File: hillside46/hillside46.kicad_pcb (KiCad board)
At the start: 2 copper layers, 142.5 x 99.9 mm, 86 parts, among them J1 Haptic, J2 TRRS, J3 Bat_Pos, J4 Bat_Neg, J5 Bat_Pos, J6 Bat_Neg, K1 SW_Key, K10 SW_Key, K11 SW_Key, K12 SW_Key, K13 SW_Key, K14 SW_Key, K15 SW_Key, K16 SW_Key, K17 SW_Key, K18 SW_Key, K19 SW_Rotary, K2 SW_Key, K20 SW_Rotary, K21 SW_Key, K22 SW_Key, K23 SW_Key, K3 SW_Key, K4 SW_Key, K5 SW_Key, K6 SW_Key, K7 SW_Key, K8 SW_Key, K9 SW_Key, SW1 SKQGAFE010, SW2 SW_Power, U1 ProMicro_r, U2 SRV05-4

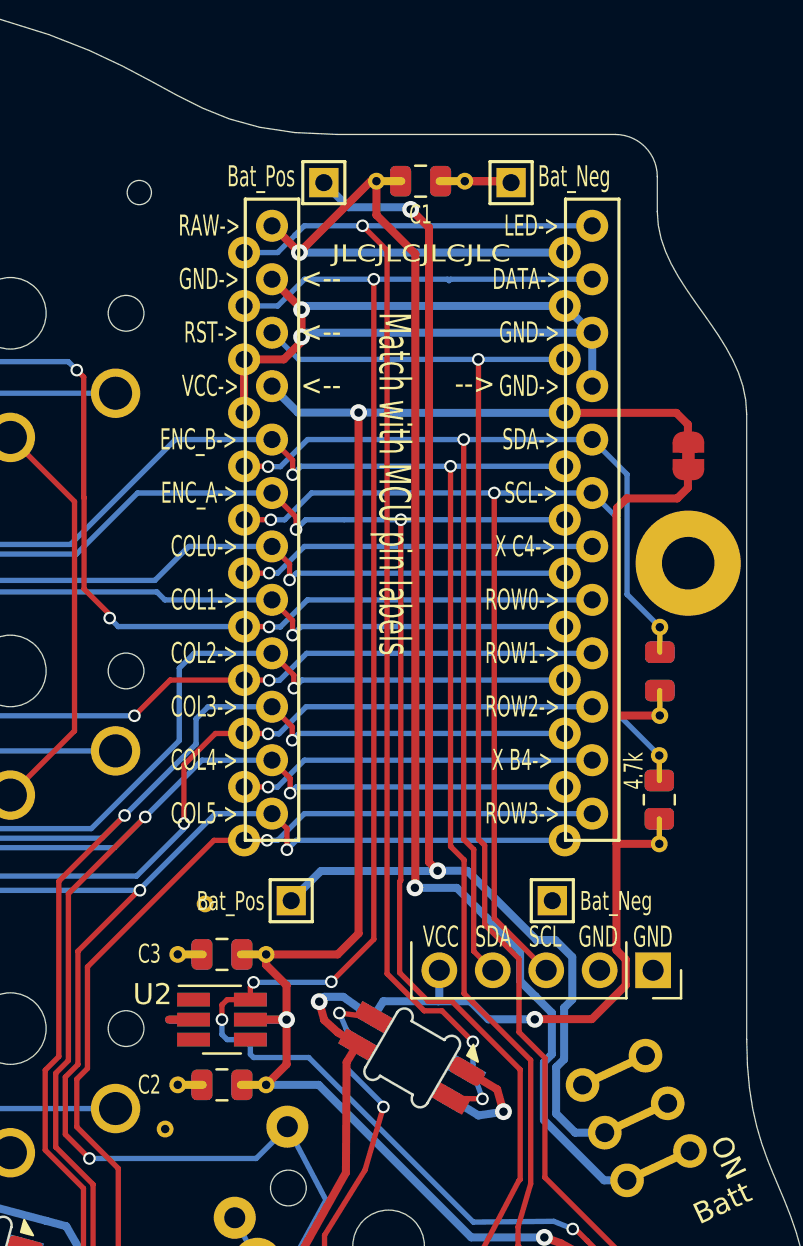
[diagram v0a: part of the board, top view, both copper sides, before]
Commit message: 46: PCB: SOT-23 has silk layout on back
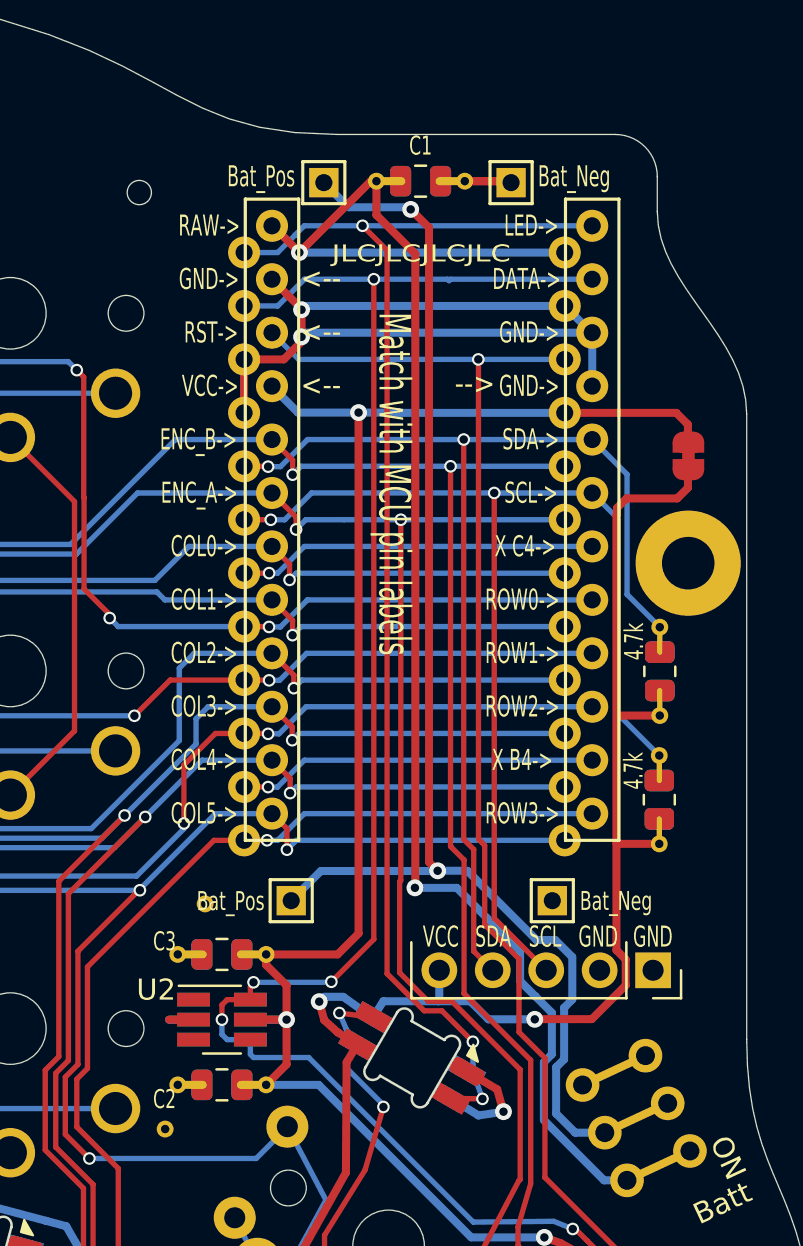
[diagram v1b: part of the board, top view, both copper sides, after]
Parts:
- R2: moved to F.Cu

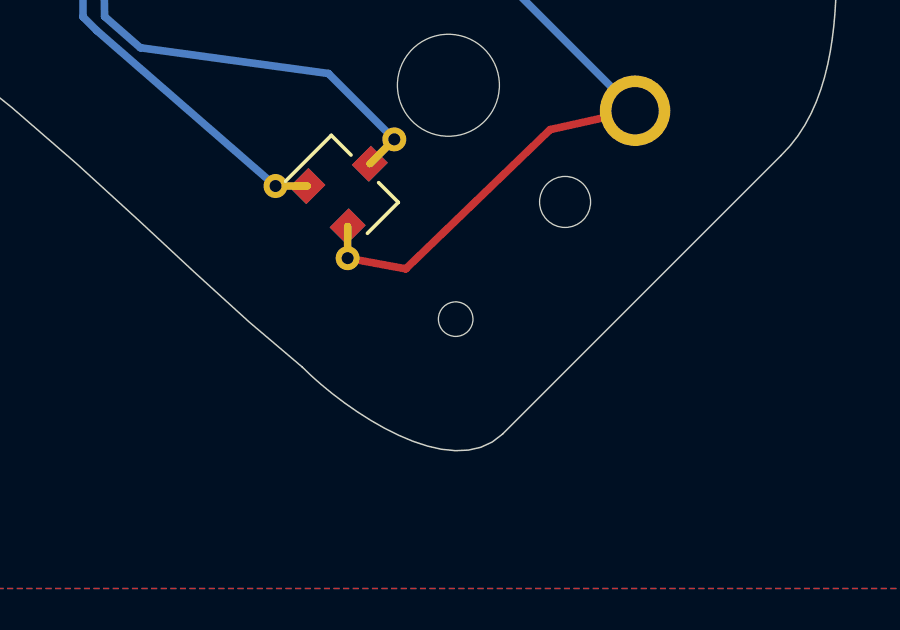
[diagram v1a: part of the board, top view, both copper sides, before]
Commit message: 46: PCB Tooling hole in more from edge
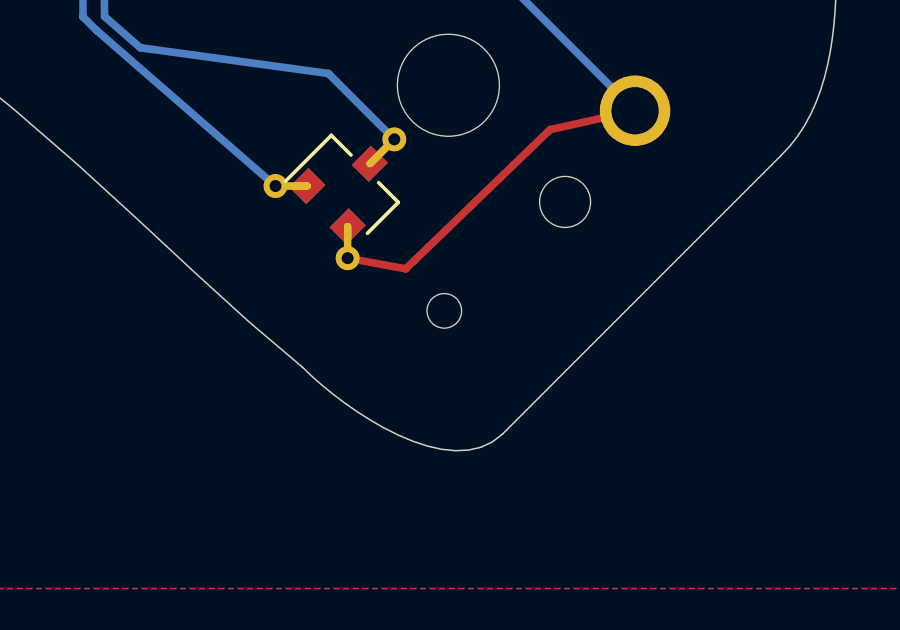
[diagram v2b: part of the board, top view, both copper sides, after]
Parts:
- moved H25 0.47 mm to (203.9, 144.0)
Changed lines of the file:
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@@
   )
   (footprint "hillside_basic:ToolingHole_1.152mm" (layer "F.Cu")
-    (at 204.258727 144.279154)
+    (at 203.879829 144.003153)
     (descr "Mounting Hole 2.1mm, no annular")
     (tags "mounting hole 2.1mm no annular")

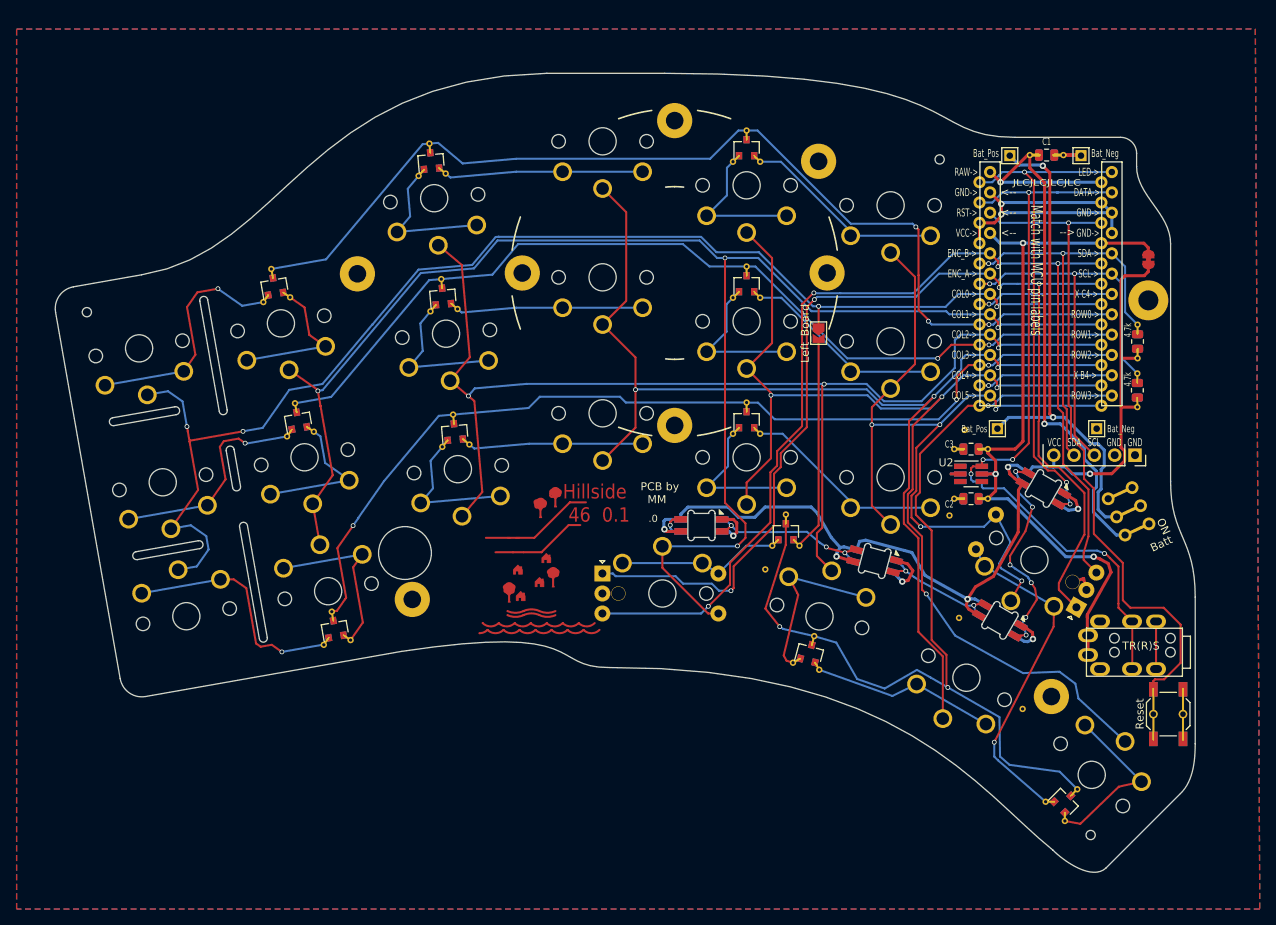
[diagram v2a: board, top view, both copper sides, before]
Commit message: 46: PCB top edge slopes at each finger. Hill like.
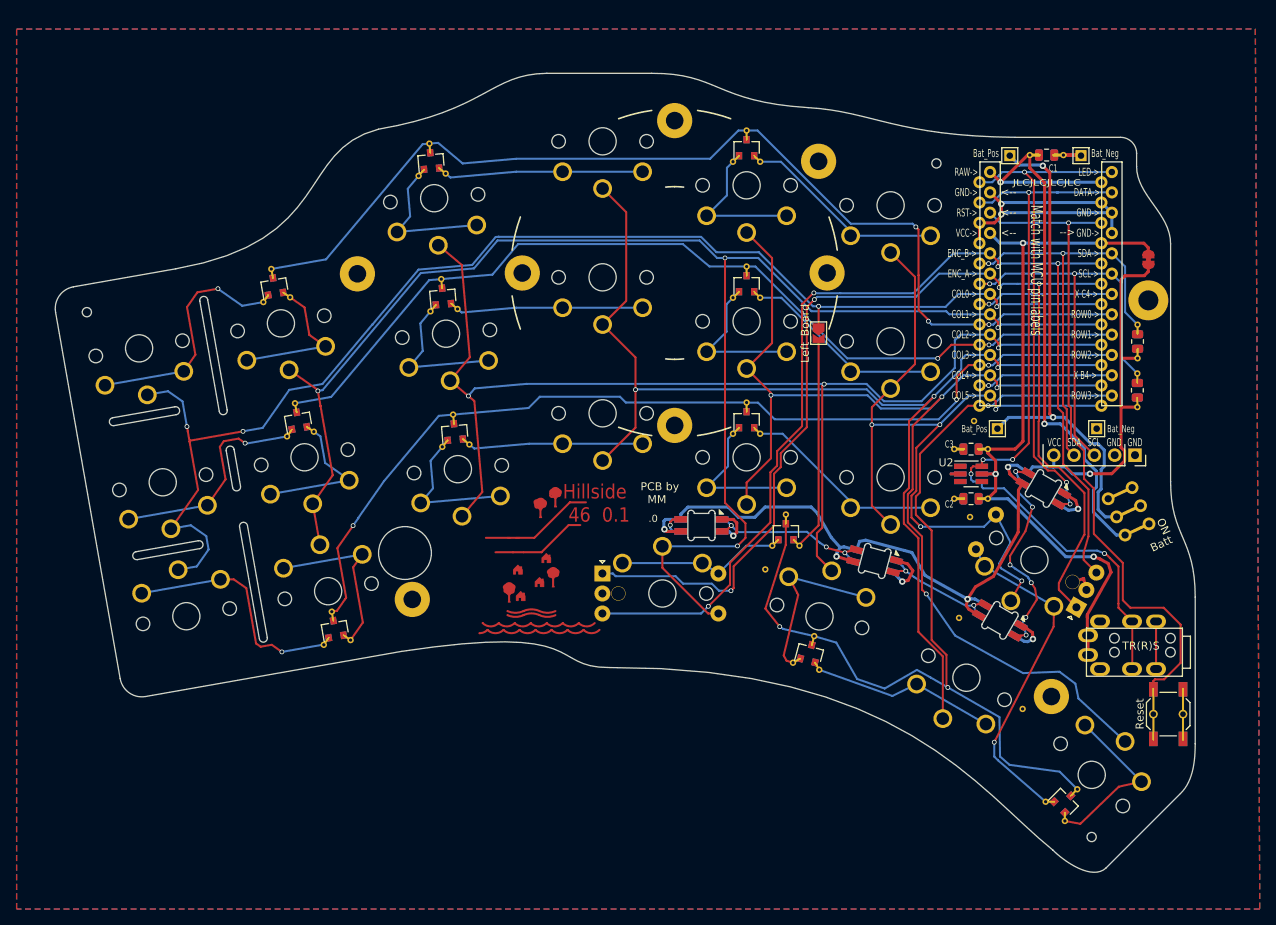
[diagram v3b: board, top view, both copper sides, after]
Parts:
- moved H9 11.0 mm to (117.8, 59.8)
- moved V1 2.58 mm to (188.8, 104.3)
- moved H17 1.79 mm to (178.7, 58.6)
- moved V2 1.62 mm to (189.3, 92.3)
- moved H20 0.68 mm to (159.0, 54.2)
- moved H23 0.64 mm to (184.6, 60.1)
- moved H25 0.28 mm to (204.0, 144.3)
- moved H15 0.20 mm to (93.2, 76.9)
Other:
- outline, holes or cut-outs redrawn
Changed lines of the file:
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@@
   )
   (footprint "hillside_basic:VIA-0.8mm" (layer "F.Cu")
-    (at 188.133108 93.367116)
+    (at 189.304829 92.253153)
     (property "Config" "do not fit")
     (property "Sheetfile" "hillside46.kicad_sch")
@@
       (effects (font (size 1 1) (thickness 0.153)))
     )
-    (fp_text value "4.7k" (at 1.420142 -1.212663 90) (layer "F.SilkS")
+    (fp_text value "4.7k" (at 1.420142 -1.212663 90) (layer "F.Fab")
       (effects (font (size 0.9 0.6) (thickness 0.15)))
     )
@@
     (property "Sheetname" "")
     (attr smd)
-    (fp_text reference "C1" (at 0 -1.68) (layer "F.SilkS")
+    (fp_text reference "C1" (at 0.829054 1.640894) (layer "F.SilkS")
       (effects (font (size 0.9 0.6) (thickness 0.15)))
     )
-    (fp_text value "4u7" (at 0 1.68) (layer "F.Fab")
+    (fp_text value "4u7" (at -1.270946 1.68) (layer "F.Fab")
       (effects (font (size 1 1) (thickness 0.15)))
     )
@@
       (effects (font (size 1 1) (thickness 0.153)))
     )
-    (fp_text value "4.7k" (at 1.370138 -1.212665 90) (layer "F.SilkS")
+    (fp_text value "4.7k" (at 1.370138 -1.212665 90) (layer "F.Fab")
       (effects (font (size 0.9 0.6) (thickness 0.15)))
     )
@@
   )
   (footprint "hillside_basic:ToolingHole_1.152mm" (layer "F.Cu")
-    (at 203.879829 144.003153)
+    (at 204.004829 144.253153)
     (descr "Mounting Hole 2.1mm, no annular")
     (tags "mounting hole 2.1mm no annular")
@@
   )
   (footprint "hillside_basic:ToolingHole_1.152mm" (layer "F.Cu")
-    (at 185.004829 59.553153)
+    (at 184.604829 60.053153)
     (descr "Mounting Hole 2.1mm, no annular")
     (tags "mounting hole 2.1mm no annular")
@@
   )
   (footprint "hillside:Bumpon" (layer "F.Cu")
-    (at 180.114829 57.493152)
+    (at 178.704829 58.603153)
     (property "Config" "do not fit")
     (property "Sheetfile" "hillside46.kicad_sch")
@@
   )
   (footprint "hillside:Bumpon" (layer "F.Cu")
-    (at 109.180815 66.623448 10)
+    (at 117.779829 59.803153 10)
     (property "Config" "do not fit")
     (property "Sheetfile" "hillside46.kicad_sch")
@@
   )
   (footprint "hillside:Bumpon" (layer "F.Cu")
-    (at 93.204829 76.653153 10)
+    (at 93.204829 76.853153 10)
     (property "Config" "do not fit")
     (property "Sheetfile" "hillside46.kicad_sch")
@@
   )
   (footprint "hillside_basic:VIA-0.8mm" (layer "F.Cu")
-    (at 186.233108 104.067117)
+    (at 188.804829 104.253153)
     (property "Config" "do not fit")
     (property "Sheetfile" "hillside46.kicad_sch")
@@
   )
   (footprint "hillside:Bumpon" (layer "F.Cu")
-    (at 159.467453 54.748763)
+    (at 159.029829 54.228153)
     (property "Config" "do not fit")
     (property "Sheetfile" "hillside46.kicad_sch")
@@
     (fp_circle (center 0 0) (end 3.95 0) (layer "User.2") (width 0.12) (fill none))
   )
-  (gr_line (start 150.625769 48.792254) (end 135.885771 48.792263) (layer "Edge.Cuts") (width 0.05))
+  (gr_line (start 149.004829 48.792254) (end 135.885771 48.792263) (layer "Edge.Cuts") (width 0.05))
   (gr_line (start 215.102248 138.826117) (end 205.821011 148.110245) (layer "Edge.Cuts") (width 0.05))
   (gr_line (start 74.498279 78.666546) (end 82.572923 124.46011) (layer "Edge.Cuts") (width 0.05))
@@
   (gr_line (start 213.875774 99.802261) (end 213.875769 70.087792) (layer "Edge.Cuts") (width 0.05))
   (gr_line (start 94.959781 91.051603) (end 92.528701 77.264297) (layer "Edge.Cuts") (width 0.05))
-  (gr_curve (pts (xy 194.425769 56.79226) (xy 182.52577 56.792257) (xy 189.425776 48.792255) (xy 150.625769 48.792254)) (layer "Edge.Cuts") (width 0.05))
+  (gr_curve (pts (xy 168.554829 53.078153) (xy 156.879829 52.353153) (xy 157.404829 48.753153) (xy 149.004829 48.792254)) (layer "Edge.Cuts") (width 0.05))
   (gr_line (start 89.590011 91.459818) (end 81.810028 92.831643) (layer "Edge.Cuts") (width 0.05))
-  (gr_curve (pts (xy 135.885771 48.792263) (xy 105.900791 49.282055) (xy 103.047523 71.140654) (xy 85.258327 73.976881)) (layer "Edge.Cuts") (width 0.05))
+  (gr_curve (pts (xy 114.854829 55.778153) (xy 104.579829 58.428153) (xy 109.354829 69.753153) (xy 89.529829 73.228153)) (layer "Edge.Cuts") (width 0.05))
   (gr_line (start 93.513517 77.090645) (end 95.94459 90.877952) (layer "Edge.Cuts") (width 0.05))
   (gr_curve (pts (xy 215.102248 138.826117) (xy 216.795771 137.202259) (xy 216.945771 134.432259) (xy 216.951097 132.583007)) (layer "Edge.Cuts") (width 0.05))
-  (gr_line (start 85.258327 73.976881) (end 76.728967 75.480796) (layer "Edge.Cuts") (width 0.05))
+  (gr_line (start 89.529829 73.228153) (end 76.728967 75.480796) (layer "Edge.Cuts") (width 0.05))
   (gr_arc (start 84.732575 109.578602) (mid 84.153228 109.172996) (end 84.558927 108.5938) (layer "Edge.Cuts") (width 0.05))
+  (gr_curve (pts (xy 194.425769 56.79226) (xy 179.604829 56.653153) (xy 176.604829 53.553153) (xy 168.554829 53.078153)) (layer "Edge.Cuts") (width 0.05))
   (gr_curve (pts (xy 199.140774 145.87226) (xy 189.808371 138.369754) (xy 179.962699 122.843559) (xy 143.688726 123.069153)) (layer "Edge.Cuts") (width 0.05))
   (gr_curve (pts (xy 213.875769 70.087792) (xy 213.875772 66.342254) (xy 209.625773 64.042258) (xy 209.625776 60.452258)) (layer "Edge.Cuts") (width 0.05))
@@
   (gr_line (start 98.482951 105.326211) (end 100.957708 119.308824) (layer "Edge.Cuts") (width 0.05))
   (gr_line (start 92.512557 108.206788) (end 84.732575 109.578602) (layer "Edge.Cuts") (width 0.05))
+  (gr_curve (pts (xy 135.885771 48.792263) (xy 128.829829 48.878153) (xy 128.379829 53.453153) (xy 114.854829 55.778153)) (layer "Edge.Cuts") (width 0.05))
   (gr_circle (center 118.172819 108.755542) (end 121.424648 108.182153) (layer "Edge.Cuts") (width 0.05) (fill none))
   (gr_arc (start 97.49814 105.499862) (mid 97.903749 104.92063) (end 98.482951 105.326211) (layer "Edge.Cuts") (width 0.05))
@@
     (members
       027cb229-6475-476f-a2db-466c6838d063
+      477e3feb-f321-4cd2-98fc-f476d7ca111e
     )
   )
@@
     (members
       1bf20e62-9fd6-4d55-b6f6-1ee95418f6c8
+      d74aae3e-825e-4f05-9f46-4b0ecb9d1578
     )
   )

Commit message: 46: PCB pinkie edge cut parallel with index column
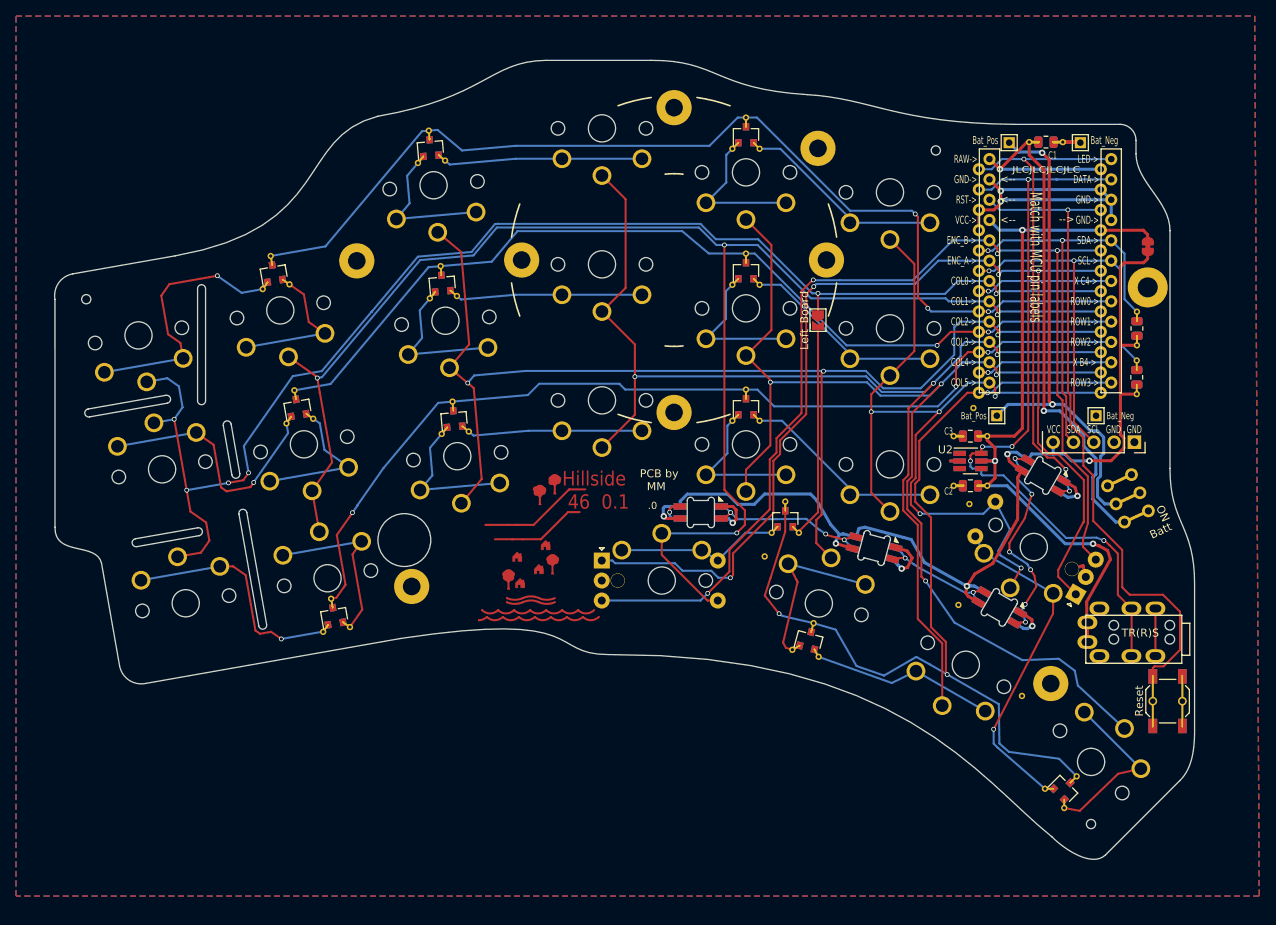
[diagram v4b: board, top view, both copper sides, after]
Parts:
- moved H13 9.42 mm to (78.9, 103.8)
- moved H10 2.31 mm to (78.7, 77.6)
- moved H19 1.62 mm to (194.8, 132.5)
- moved H15 1.62 mm to (93.1, 75.2)
- moved H16 1.62 mm to (203.0, 140.9)
- moved K23 1.62 mm to (203.9, 134.9)
- moved H23 1.62 mm to (184.5, 58.4)
- moved D15 1.62 mm to (160.8, 90.5)
- moved K20 1.62 mm to (150.3, 116.7)
- moved SW2 1.62 mm to (208.5, 101.9)
- moved V3 1.62 mm to (187.4, 115.2)
- moved D11 1.62 mm to (122.8, 75.0)
- moved K9 1.62 mm to (123.2, 79.7)
- moved V5 1.62 mm to (163.1, 109.2)
- moved D10 1.62 mm to (104.7, 90.5)
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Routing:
- net col0: track 166.7 -> 172.6 mm, vias 4 -> 6
- net Net-(D10-Pad1): track 17.2 -> 21.4 mm
- net Net-(D7-Pad1): track 19.8 -> 23.0 mm
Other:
- outline, holes or cut-outs redrawn
- board text removed: "CUT"
